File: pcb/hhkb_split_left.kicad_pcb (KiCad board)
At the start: 2 copper layers, 140.4 x 97.4 mm, 65 parts, among them SW1 Esc, SW10 E, SW11 R, SW12 T, SW13 Ctrl, SW14 A, SW15 S, SW16 D, SW17 F, SW18 G, SW19 Shift, SW2 1, SW20 Z, SW21 X, SW22 C, SW23 V, SW24 B, SW25 Alt, SW26 Meta, SW27 L-Space, SW3 2, SW4 3, SW5 4, SW6 5, SW7 Tab, SW8 Q, SW9 W, U1 74LVC595

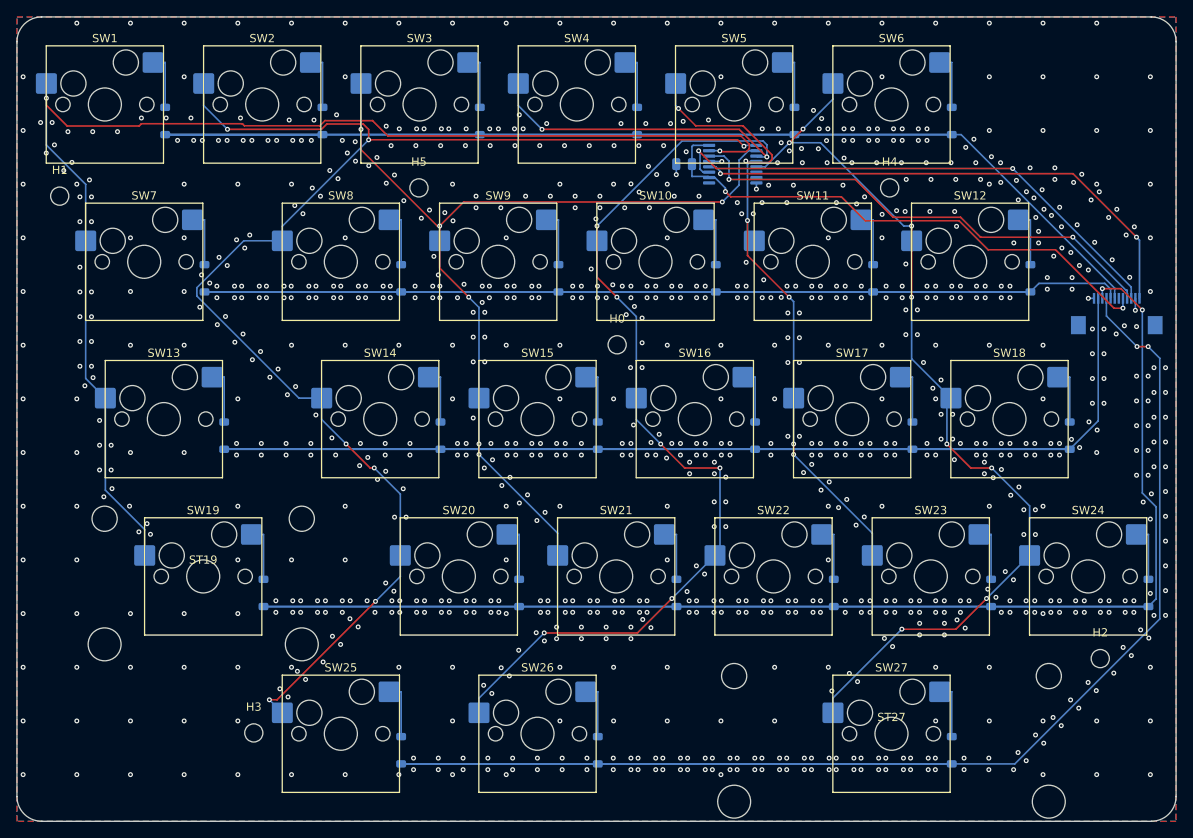
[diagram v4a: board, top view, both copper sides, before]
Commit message: 子基板の配線を外周へ逃がし、電源部の向きを流れに合わせた
利用者が絵で示した「電源は盤面の外周を使い、中央を空ける」という
方針を実装した回。**私は数字だけ追っていて、絵を見た利用者の指摘の
ほうが毎回早く核心に届いた。**

■ 外周レーン（利用者「両側 2 ピンぐらいは外側から回せるのでは」）

  XIAO のパッド列（±7.62）の外に **2.03mm** ある。ここへ 2 本/側を
  逃がし、内側レーンを 5 本 → 2 本に減らした。

  ⚠️ **刻みはビアの径で決まる。**最初 0.4mm（配線の幅）で 3 本置いて
  DRC 13 件。φ0.6 + クリアランス 0.2 = **0.80mm 必要**で 2 本/側が上限。

  ⚠️ **ビアを省いて裏面のまま走らせる案は駄目。**間隔 0.40mm で 3 本
  入る（外周に裏面部品は無い）が、**層の分離を失う**。内側レーンへ
  向かう横枝は B.Cu なので、外側も B.Cu だと必ず交差する（実測 12 件）。
  **ビアは無駄ではなく、層を分けるために要る。**

■ 真下パス（利用者「D6/D7 は横向きでなく下向きに伸ばせる」）

  FFC に最も近い 1 本は、パッド列の x のまま真下へ降ろす。
  レーンもビアも使わない。ROW2 18.9→16.8mm、CS 18.4→16.2mm。

  ⚠️ 条件を `|x| > 7.0` で書いて**全パッドが該当**し、20mm の配線が
  盤面を横断して DRC 38 件。正しくは「その列で FFC に最も近い 1 本」
  ＝ i == 0。

■ 部品の向き（利用者「バルクの向きが逆」「電源周りこんな感じで」）

  - C_BULK: 縦置き（x 方向 1.4mm 節約）＋ **+90°**。XIAO は 3V3 が
    手前(9.59)・GND が奥(12.13) なので、同じ並びにして平行に届かせる
  - R_LO: 180°。SENSE が R_HI 側（左）を向き、分圧の中点が隣り合う
  - SW_PWR: 中央の縦帯（x ±0.9）を空ける。GND スティッチングが使う

■ 配線長

  子基板の合計 218.5 → **205.1mm**

DRC: 左 違反3/未配線0 / 右 違反2/未配線0 / 子基板 違反6/未配線1
（主基板は**両方とも未配線 0**。子基板の 6 件は下記）
test_circuit・test_daughterboard・test_keyscan・test_schematic・
test_pinmap = 81 件通過。**pytest tools 全体は未実行。**

Co-Authored-By: Claude Opus 5 (1M context) <noreply@anthropic.com>
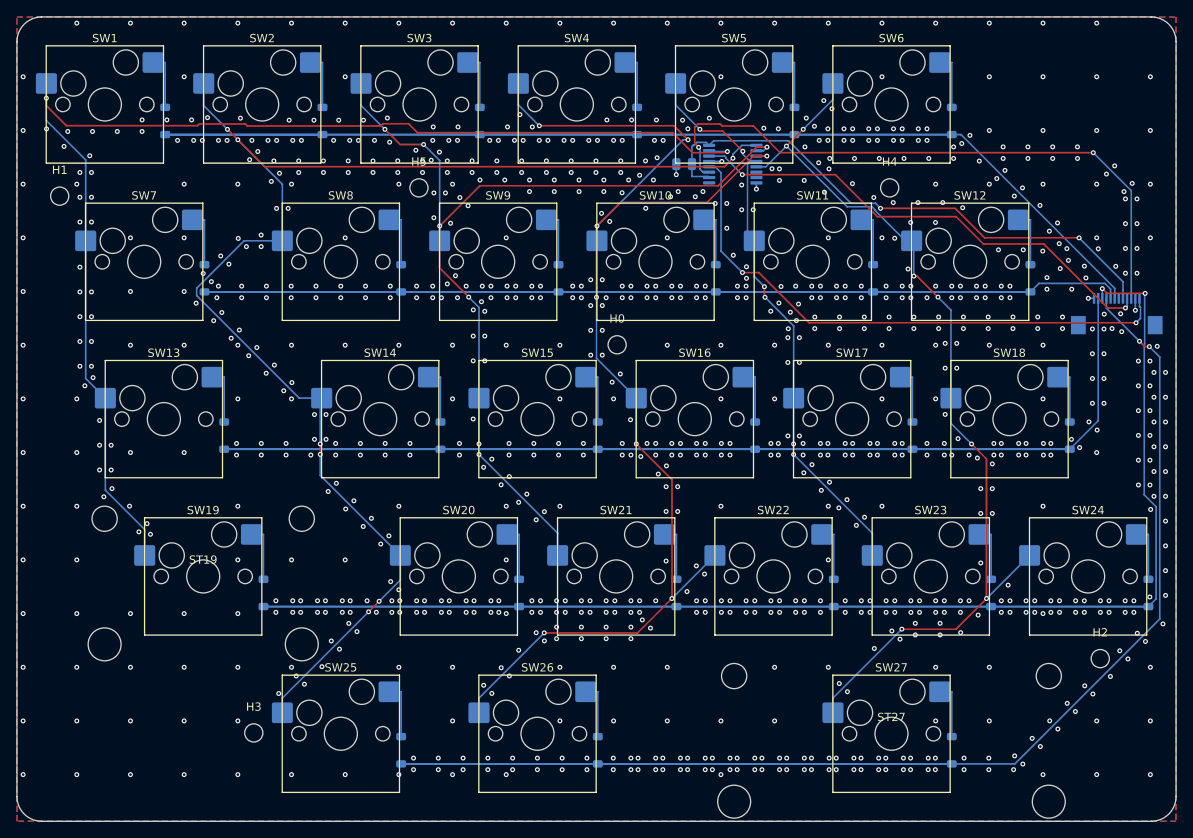
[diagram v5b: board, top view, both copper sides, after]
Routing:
- net SPI_SCK: track 64.1 -> 76.0 mm
- net COL4: track 78.8 -> 69.5 mm
- net COL0: track 156.3 -> 150.5 mm
- net CS: track 63.0 -> 68.3 mm
- net COL1: track 173.5 -> 170.5 mm
- net COL2: track 112.9 -> 115.5 mm, vias 6 -> 7
- net COL3: track 151.3 -> 153.8 mm
- net V3V3: track 66.0 -> 67.6 mm
- net ROW3: track 258.4 -> 259.9 mm
- net COL5: track 115.8 -> 114.6 mm, vias 8 -> 7
- net GND: vias 1002 -> 1027

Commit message: 左右の基板を、前のセッションが引き直した状態で記録する
作業ツリーに残っていた left / right の現物を入れる。ROW の割り当てを
変えたあとの再配線で、配線とビアが引き直されている（左はビア 79 本、
右は 41 本が別の位置へ）。route_right.json の unconnected も 0 → 1 に
なっており、記録と現物の sha256 は一致している。

  left   違反 0 / 未配線 0 / 警告 35
  right  違反 0 / 未配線 1 / 警告 48

⚠️ **この 2 枚には 8ef4720 のコード変更が反映されていない。**
浮いた GND の連結成分での判定、穴を障害物に入れる修正、ELEC_REF への
J_MAIN 追加は、いずれも次に gen_pcb → autoroute を回したときに効く。
right の未配線 1 件（U1 の GND パッド 13 が浮いたベタ経由でしか
出ていない）も、そのときに解消するかを見る。

基板そのものを管理するのは、autoroute が再現しないため。実測すると
unrouted は UUID と並び順を除いて完全に一致するが、配線後は
Freerouting が毎回違う経路を引く。**DRC 0 を確認した現物は、
捨てると復元できない。**

Co-Authored-By: Claude Opus 5 (1M context) <noreply@anthropic.com>
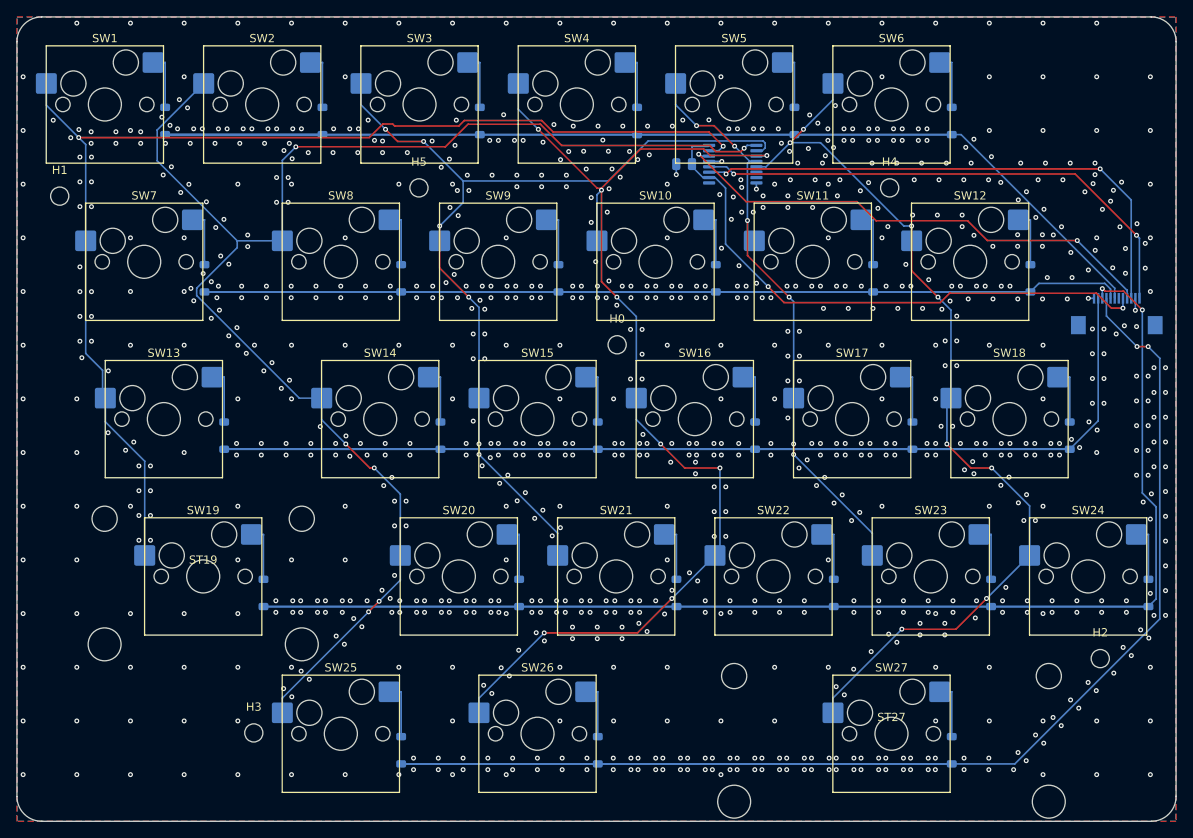
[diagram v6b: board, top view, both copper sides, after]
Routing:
- net COL3: track 153.8 -> 137.8 mm
- net SPI_SCK: track 76.0 -> 64.9 mm
- net COL1: track 170.5 -> 178.7 mm, vias 7 -> 6
- net COL0: track 150.5 -> 144.4 mm
- net CS: track 68.3 -> 63.0 mm
- net COL4: track 69.5 -> 72.1 mm
- net V3V3: track 67.6 -> 70.0 mm
- net COL2: track 115.5 -> 113.5 mm, vias 7 -> 6
- net SPI_MOSI: track 59.4 -> 61.0 mm
- net ROW3: track 259.9 -> 258.4 mm
- net COL5: track 114.6 -> 115.8 mm, vias 7 -> 8
- net GND: vias 1027 -> 949
